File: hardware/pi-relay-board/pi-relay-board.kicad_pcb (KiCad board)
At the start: 2 copper layers, 101.9 x 59.1 mm, 41 parts, among them J1 Raspberry_Pi_2_3, J10 Conn_01x03_Socket, J11 Conn_01x03_Socket, J2 Conn_01x03_Socket, J3 Conn_01x03_Socket, J4 Conn_01x03_Socket, J5 Conn_01x03_Socket, J6 Conn_01x03_Socket, J7 Conn_01x03_Socket, J8 Conn_01x03_Socket, J9 Conn_01x03_Socket, K1 TIANBO-HJR-4102-L, K10 TIANBO-HJR-4102-L, K2 TIANBO-HJR-4102-L, K3 TIANBO-HJR-4102-L, K4 TIANBO-HJR-4102-L, K5 TIANBO-HJR-4102-L, K6 TIANBO-HJR-4102-L, K7 TIANBO-HJR-4102-L, K8 TIANBO-HJR-4102-L, K9 TIANBO-HJR-4102-L, Q11 BC847, Q12 BC847, Q13 BC847, Q14 BC847, Q15 BC847, Q16 BC847, Q17 BC847, Q18 BC847, Q19 BC847, Q20 BC847

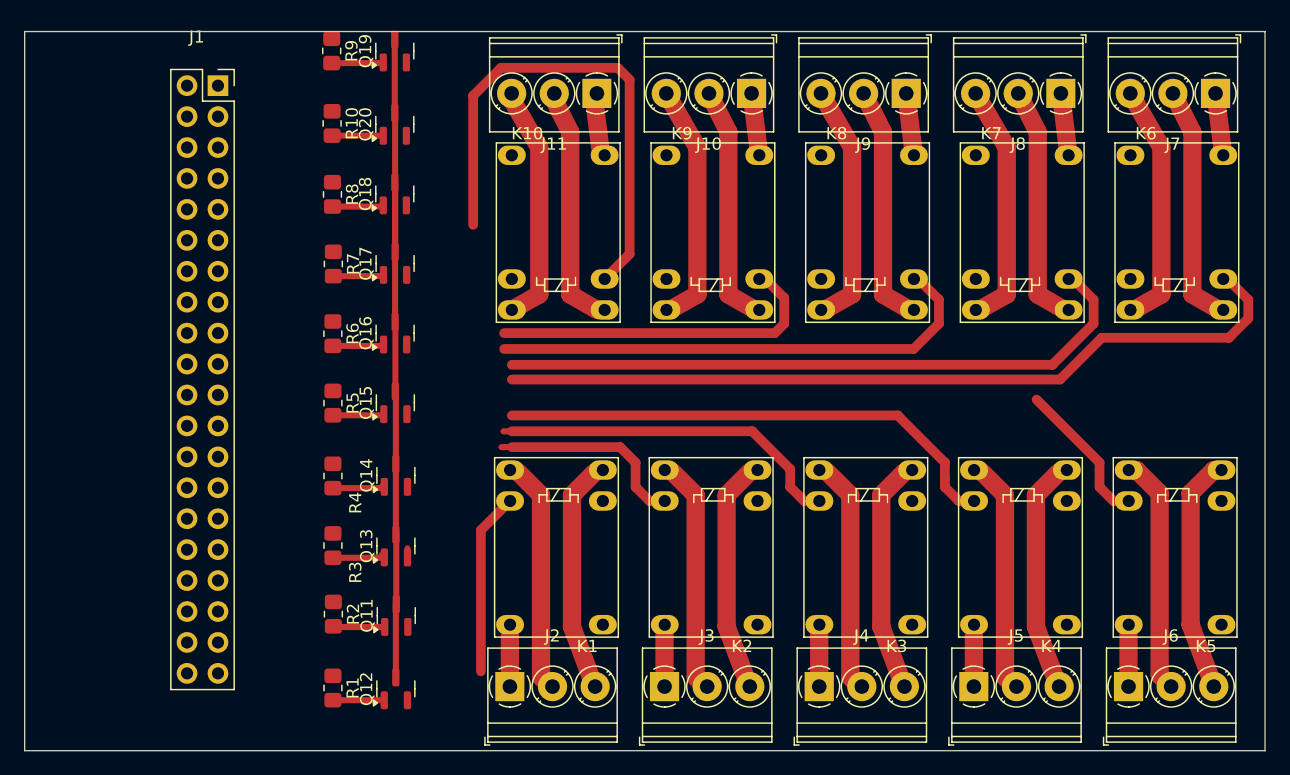
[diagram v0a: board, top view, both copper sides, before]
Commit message: hardware: change to tht
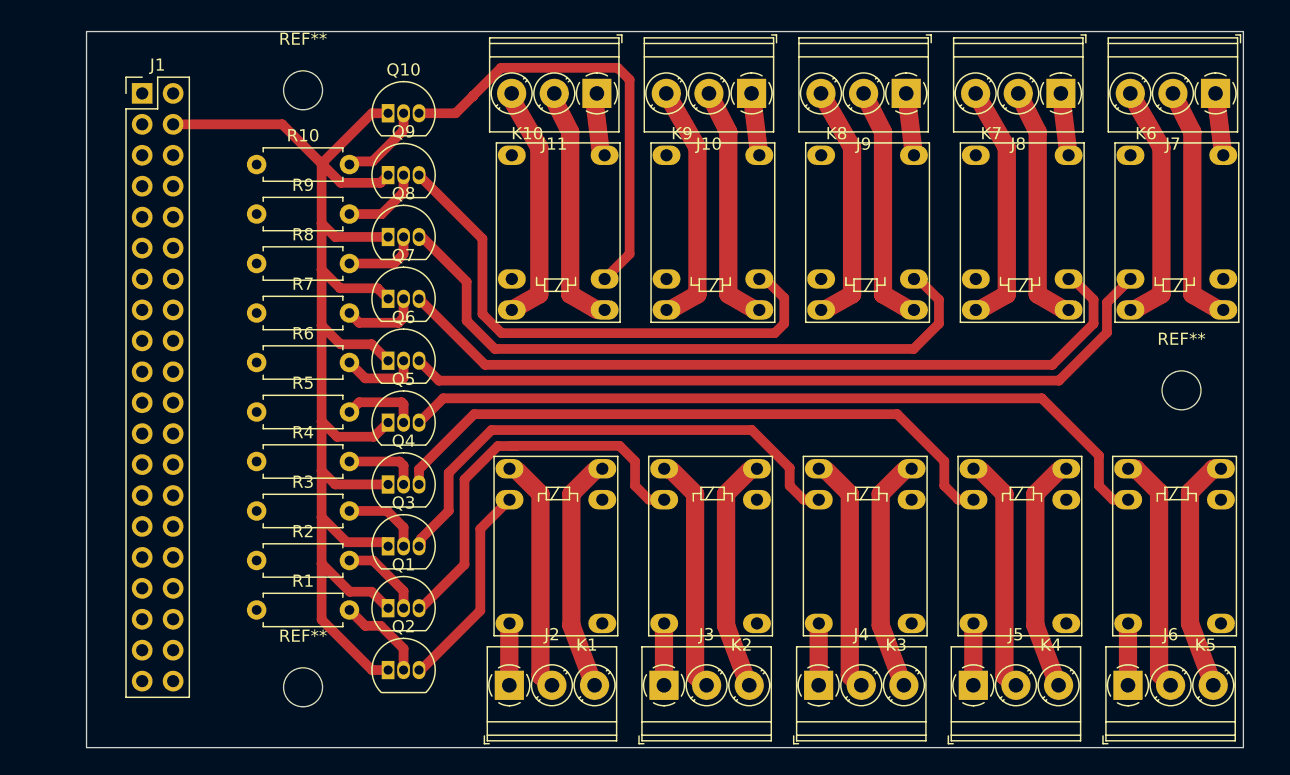
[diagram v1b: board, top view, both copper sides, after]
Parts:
- removed Q11, Q12, Q13, Q14, Q15, Q16, Q17, Q18, Q19, Q20: BC847, Package_TO_SOT_SMD:SOT-23
- added Q1: BC547, Package_TO_SOT_THT:TO-92_Inline, F.Cu at (173.4, 85.5)
- added Q10: BC547, Package_TO_SOT_THT:TO-92_Inline, F.Cu at (173.4, 44.8)
- added Q2: BC547, Package_TO_SOT_THT:TO-92_Inline, F.Cu at (173.4, 90.5)
- added Q3: BC547, Package_TO_SOT_THT:TO-92_Inline, F.Cu at (173.4, 80.4)
- added Q4: BC547, Package_TO_SOT_THT:TO-92_Inline, F.Cu at (173.4, 75.3)
- added Q5: BC547, Package_TO_SOT_THT:TO-92_Inline, F.Cu at (173.4, 70.2)
- added Q6: BC547, Package_TO_SOT_THT:TO-92_Inline, F.Cu at (173.4, 65.1)
- added Q7: BC547, Package_TO_SOT_THT:TO-92_Inline, F.Cu at (173.4, 60.0)
- added Q8: BC547, Package_TO_SOT_THT:TO-92_Inline, F.Cu at (173.4, 55.0)
- added Q9: BC547, Package_TO_SOT_THT:TO-92_Inline, F.Cu at (173.4, 49.9)
- added REF**: MountingHole_3.2mm_M3, MountingHole:MountingHole_3.2mm_M3, F.Cu at (166.4, 42.9)
- added REF**: MountingHole_3.2mm_M3, MountingHole:MountingHole_3.2mm_M3, F.Cu at (238.5, 67.6)
- added REF**: MountingHole_3.2mm_M3, MountingHole:MountingHole_3.2mm_M3, F.Cu at (166.4, 91.9)
- J1: footprint custom:Raspberry Connector -> Connector_PinHeader_2.54mm:PinHeader_2x20_P2.54mm_Vertical
- R1, R10, R2, R3, R4, R5, R6, R7, R8, R9: footprint Resistor_SMD:R_0805_2012Metric_Pad1.20x1.40mm_HandSolder -> Resistor_THT:R_Axial_DIN0207_L6.3mm_D2.5mm_P7.62mm_Horizontal
- moved J1 24.4 mm to (153.2, 43.2)
- moved R9 14.7 mm to (162.6, 53.1), turned to 0 degrees
- moved R1 8.96 mm to (162.6, 85.6), turned to 0 degrees
- moved R8 8.43 mm to (162.6, 57.1), turned to 0 degrees
- moved R2 7.69 mm to (162.6, 81.5), turned to 0 degrees
- moved R7 7.48 mm to (162.6, 61.2), turned to 0 degrees
- moved R10 7.05 mm to (162.6, 49.0), turned to 0 degrees
- moved R3 6.88 mm to (162.6, 77.5), turned to 0 degrees
- moved R6 6.69 mm to (162.6, 65.3), turned to 0 degrees
- moved R4 6.38 mm to (162.6, 73.4), turned to 0 degrees
- moved R5 6.31 mm to (162.6, 69.3), turned to 0 degrees
- moved J2 0.12 mm to (183.3, 91.8)
- moved J3 0.12 mm to (196.0, 91.8)
- moved J4 0.12 mm to (208.7, 91.8)
- moved J5 0.12 mm to (221.4, 91.8)
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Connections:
- J1 pad 11: /GPIO_1 -> /GPIO_5
- J1 pad 13: /GPIO_4 -> /GPIO_2
- J1 pad 15: /GPIO_3 -> /GPIO_6
- J1 pad 16: /GPIO_2 -> /GPIO
- J1 pad 18: /GPIO_7 -> /GPIO_8
- J1 pad 22: /GPIO_5 -> /GPIO_7
- J1 pad 29: /GPIO -> /GPIO_3
- J1 pad 31: /GPIO_8 -> /GPIO_4
- J1 pad 37: /GPIO_6 -> /GPIO_1
- K1 pad 5: unconnected-(K1-Pad5) -> Net-(Q2-E)
- K1 pad 8: Net-(Q12-E) -> Net-(Q2-E)
- K10 pad 5: unconnected-(K10-Pad5) -> Net-(Q10-E)
- K10 pad 8: Net-(Q20-E) -> Net-(Q10-E)
- K2 pad 5: unconnected-(K2-Pad5) -> Net-(Q1-E)
- K2 pad 8: Net-(Q11-E) -> Net-(Q1-E)
- K3 pad 5: unconnected-(K3-Pad5) -> Net-(Q3-E)
- K3 pad 8: Net-(Q13-E) -> Net-(Q3-E)
- K4 pad 5: unconnected-(K4-Pad5) -> Net-(Q4-E)
- K4 pad 8: Net-(Q14-E) -> Net-(Q4-E)
- K5 pad 5: unconnected-(K5-Pad5) -> Net-(Q5-E)
- K5 pad 8: Net-(Q15-E) -> Net-(Q5-E)
- K6 pad 5: unconnected-(K6-Pad5) -> Net-(Q6-E)
- K6 pad 8: Net-(Q16-E) -> Net-(Q6-E)
- K7 pad 5: unconnected-(K7-Pad5) -> Net-(Q7-E)
- K7 pad 8: Net-(Q17-E) -> Net-(Q7-E)
- K8 pad 5: unconnected-(K8-Pad5) -> Net-(Q8-E)
- K8 pad 8: Net-(Q18-E) -> Net-(Q8-E)
- K9 pad 5: unconnected-(K9-Pad5) -> Net-(Q9-E)
- K9 pad 8: Net-(Q19-E) -> Net-(Q9-E)
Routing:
- net Net-(Q16-E): track 66.8 -> 0.00 mm
- net Net-(Q6-E): track 0.00 -> 64.4 mm
- net Net-(Q5-E): track 0.00 -> 64.0 mm
- net Net-(Q7-E): track 0.00 -> 63.7 mm
- net +5V: track 58.2 -> 116.6 mm
- net Net-(Q17-E): track 53.9 -> 0.00 mm
- net Net-(Q8-E): track 0.00 -> 53.8 mm
- net Net-(Q4-E): track 0.00 -> 52.7 mm
- net Net-(Q9-E): track 0.00 -> 44.1 mm
- net Net-(Q20-E): track 42.7 -> 0.00 mm
- net Net-(Q3-E): track 0.00 -> 42.1 mm
- net Net-(Q14-E): track 42.0 -> 0.00 mm
- net Net-(Q18-E): track 41.3 -> 0.00 mm
- net Net-(Q10-E): track 0.00 -> 37.2 mm
- net Net-(Q1-E): track 0.00 -> 33.1 mm
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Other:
- board size 101.9 x 59.1 mm -> 95 x 58.8 mm

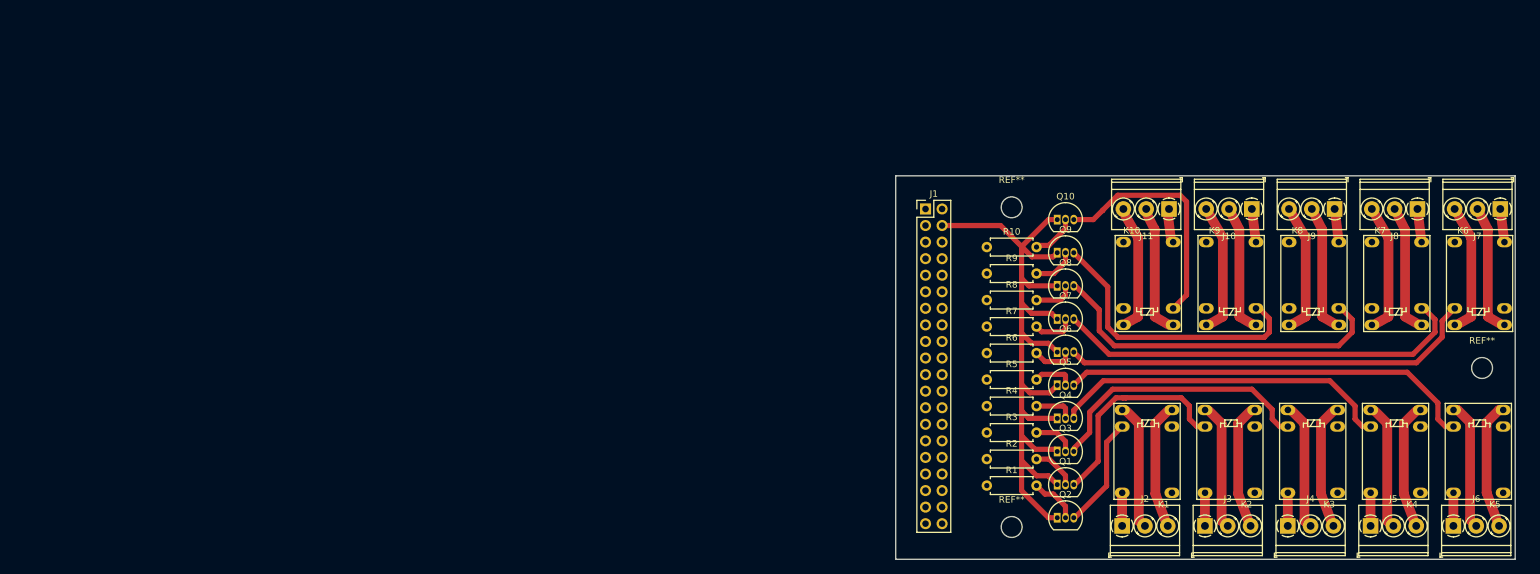
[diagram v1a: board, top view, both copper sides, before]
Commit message: feat: pcb bc547 footprint, laser image
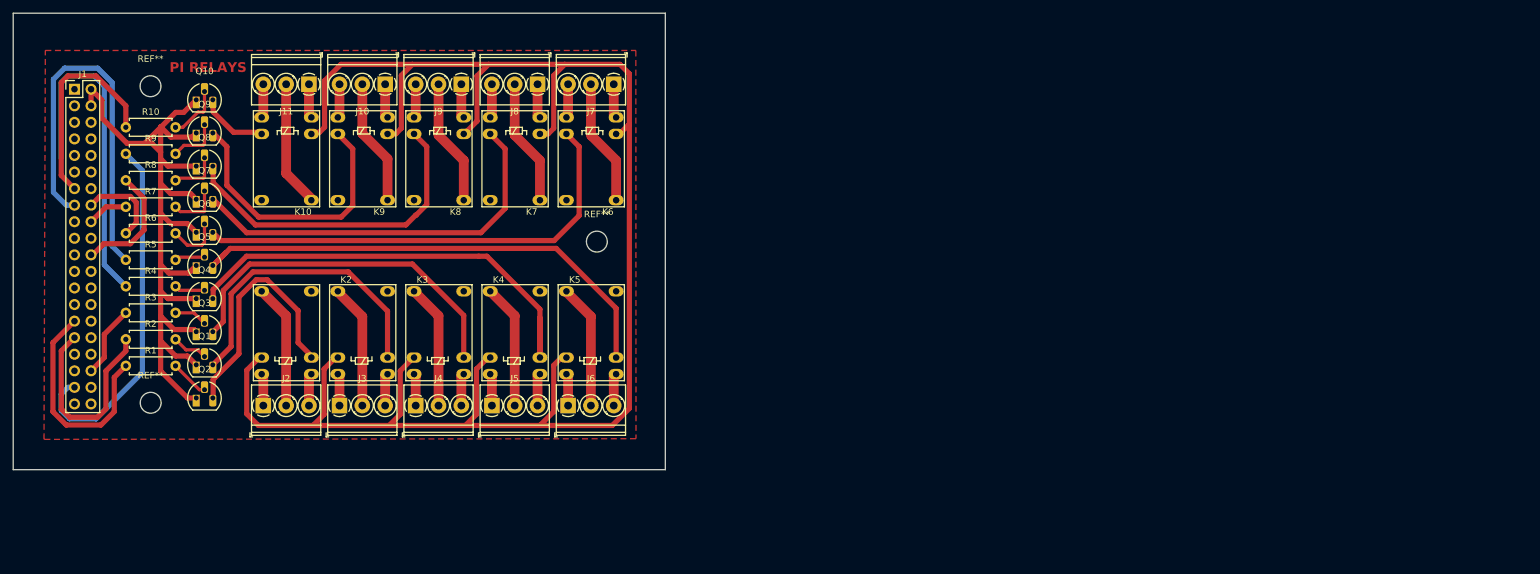
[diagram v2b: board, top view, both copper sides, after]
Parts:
- Q1, Q10, Q2, Q3, Q4, Q5, Q6, Q7, Q8, Q9: footprint Package_TO_SOT_THT:TO-92_Inline -> Package_TO_SOT_THT:TO-92_HandSolder
- moved K5 146.9 mm to (98.1, 55.8), turned to 0 degrees
- moved K4 145.9 mm to (86.4, 55.8), turned to 0 degrees
- moved K3 144.9 mm to (74.7, 55.8), turned to 0 degrees
- moved K2 144.0 mm to (63.0, 55.8), turned to 0 degrees
- moved K1 143.0 mm to (51.4, 55.8), turned to 0 degrees
- moved J7 137.3 mm to (105.3, 24.1)
- moved REF** 137.1 mm to (102.8, 48.2)
- moved J6 137.0 mm to (98.3, 73.3)
- moved J8 136.3 mm to (93.7, 24.1)
- moved J5 136.0 mm to (86.7, 73.3)
- moved J9 135.3 mm to (82.0, 24.1)
- moved J4 135.0 mm to (75.0, 73.3)
- moved J10 134.3 mm to (70.3, 24.1)
- moved J3 134.0 mm to (63.3, 73.3)
- moved REF** 133.4 mm to (34.3, 72.9)
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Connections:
- J1 pad 11: /GPIO_5 -> /Relay Pin 4/K
- J1 pad 13: /GPIO_2 -> /Relay Pin 10/K
- J1 pad 15: /GPIO_6 -> /Relay Pin 5/K
- J1 pad 16: /GPIO -> /Relay Pin 6/K
- J1 pad 18: /GPIO_8 -> /Relay Pin 7/K
- J1 pad 22: /GPIO_7 -> /Relay Pin 8/K
- J1 pad 29: /GPIO_3 -> /Relay Pin 1/K
- J1 pad 31: /GPIO_4 -> /Relay Pin 2/K
- J1 pad 37: /GPIO_1 -> /Relay Pin 9/K
- K1 pad 1: (no net) -> Net-(J2-Pin_2)
- K1 pad 12: Net-(J2-Pin_1) -> (no net)
- K1 pad 5: Net-(Q2-E) -> GND
- K1 pad 6: Net-(J2-Pin_3) -> Net-(J2-Pin_1)
- K1 pad 7: Net-(J2-Pin_2) -> Net-(J2-Pin_3)
- K10 pad 1: (no net) -> Net-(J11-Pin_2)
- K10 pad 12: Net-(J11-Pin_1) -> (no net)
- K10 pad 5: Net-(Q10-E) -> GND
- K10 pad 6: Net-(J11-Pin_3) -> Net-(J11-Pin_1)
- K10 pad 7: Net-(J11-Pin_2) -> Net-(J11-Pin_3)
- K2 pad 1: (no net) -> Net-(J3-Pin_2)
- K2 pad 12: Net-(J3-Pin_1) -> (no net)
- K2 pad 5: Net-(Q1-E) -> GND
- K2 pad 6: Net-(J3-Pin_3) -> Net-(J3-Pin_1)
- K2 pad 7: Net-(J3-Pin_2) -> Net-(J3-Pin_3)
- K3 pad 1: (no net) -> Net-(J4-Pin_2)
- K3 pad 12: Net-(J4-Pin_1) -> (no net)
- K3 pad 5: Net-(Q3-E) -> GND
- K3 pad 6: Net-(J4-Pin_3) -> Net-(J4-Pin_1)
- K3 pad 7: Net-(J4-Pin_2) -> Net-(J4-Pin_3)
- K4 pad 1: (no net) -> Net-(J5-Pin_2)
- K4 pad 12: Net-(J5-Pin_1) -> (no net)
- K4 pad 5: Net-(Q4-E) -> GND
- K4 pad 6: Net-(J5-Pin_3) -> Net-(J5-Pin_1)
- K4 pad 7: Net-(J5-Pin_2) -> Net-(J5-Pin_3)
- K5 pad 1: (no net) -> Net-(J6-Pin_2)
- K5 pad 12: Net-(J6-Pin_1) -> (no net)
- K5 pad 5: Net-(Q5-E) -> GND
- K5 pad 6: Net-(J6-Pin_3) -> Net-(J6-Pin_1)
- K5 pad 7: Net-(J6-Pin_2) -> Net-(J6-Pin_3)
- K6 pad 1: (no net) -> Net-(J7-Pin_2)
- K6 pad 12: Net-(J7-Pin_1) -> (no net)
- K6 pad 5: Net-(Q6-E) -> GND
- K6 pad 6: Net-(J7-Pin_3) -> Net-(J7-Pin_1)
- K6 pad 7: Net-(J7-Pin_2) -> Net-(J7-Pin_3)
- K7 pad 1: (no net) -> Net-(J8-Pin_2)
- K7 pad 12: Net-(J8-Pin_1) -> (no net)
- K7 pad 5: Net-(Q7-E) -> GND
- K7 pad 6: Net-(J8-Pin_3) -> Net-(J8-Pin_1)
- K7 pad 7: Net-(J8-Pin_2) -> Net-(J8-Pin_3)
- K8 pad 1: (no net) -> Net-(J9-Pin_2)
- K8 pad 12: Net-(J9-Pin_1) -> (no net)
- K8 pad 5: Net-(Q8-E) -> GND
- K8 pad 6: Net-(J9-Pin_3) -> Net-(J9-Pin_1)
- K8 pad 7: Net-(J9-Pin_2) -> Net-(J9-Pin_3)
- K9 pad 1: (no net) -> Net-(J10-Pin_2)
- K9 pad 12: Net-(J10-Pin_1) -> (no net)
- K9 pad 5: Net-(Q9-E) -> GND
- K9 pad 6: Net-(J10-Pin_3) -> Net-(J10-Pin_1)
- K9 pad 7: Net-(J10-Pin_2) -> Net-(J10-Pin_3)
- R1 pad 1: /Relay Pin 2/K1 -> /Relay Pin 1/K
- R10 pad 1: /Relay Pin 10/K1 -> /Relay Pin 10/K
- R2 pad 1: /Relay Pin 1/K1 -> /Relay Pin 2/K
- R3 pad 1: /Relay Pin 3/K1 -> /GPIO16
- R4 pad 1: /Relay Pin 4/K1 -> /Relay Pin 4/K
- R5 pad 1: /Relay Pin 5/K1 -> /Relay Pin 5/K
- R6 pad 1: /Relay Pin 6/K1 -> /Relay Pin 6/K
- R7 pad 1: /Relay Pin 7/K1 -> /Relay Pin 7/K
- R8 pad 1: /Relay Pin 8/K1 -> /Relay Pin 8/K
- R9 pad 1: /Relay Pin 9/K1 -> /Relay Pin 9/K
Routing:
- net GND: track 0.00 -> 269.3 mm
- net /Relay Pin 5/K: track 0.00 -> 60.1 mm
- net /Relay Pin 9/K: track 0.00 -> 55.5 mm
- net /Relay Pin 4/K: track 0.00 -> 51.4 mm
- net /Relay Pin 1/K: track 0.00 -> 34.1 mm
- net /Relay Pin 10/K: track 0.00 -> 32.6 mm
- net /Relay Pin 2/K: track 0.00 -> 31.6 mm
- net Net-(Q10-E): track 37.2 -> 10.6 mm
- net Net-(Q2-E): track 17.0 -> 37.2 mm
- net /Relay Pin 8/K: track 0.00 -> 18.5 mm
- net Net-(Q4-E): track 52.7 -> 70.5 mm
- net Net-(J7-Pin_3): track 20.1 -> 5.19 mm
- net Net-(J11-Pin_3): track 19.8 -> 5.19 mm
- net Net-(J9-Pin_3): track 19.8 -> 5.19 mm
- net Net-(J10-Pin_3): track 19.8 -> 5.19 mm
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- added copper zone on F.Cu, net GND
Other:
- board size 95 x 58.8 mm -> 100 x 70 mm
- board text added: "PI RELAYS"

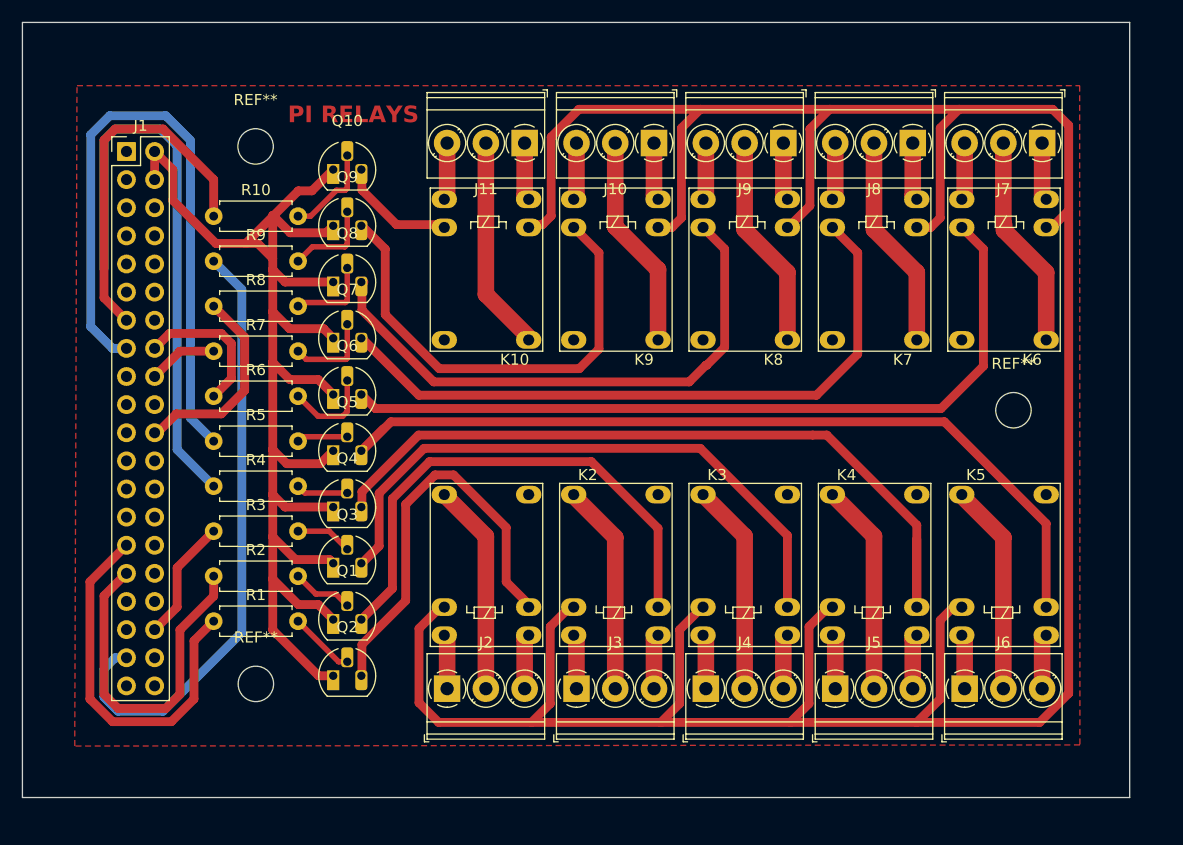
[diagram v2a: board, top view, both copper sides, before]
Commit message: fix: laser image scaling
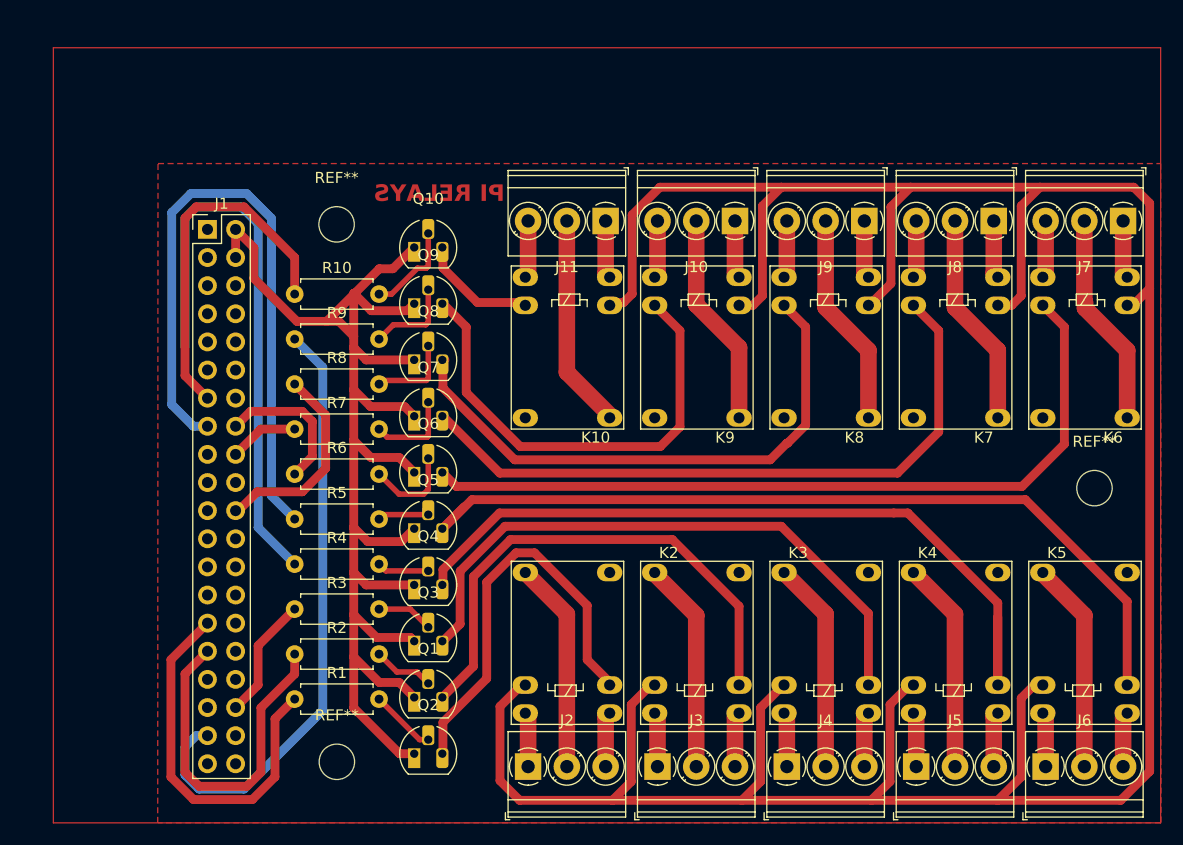
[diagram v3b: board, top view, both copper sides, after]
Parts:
- moved J7 10.1 mm to (112.7, 31.1)
- moved J8 10.1 mm to (101.0, 31.1)
- moved J9 10.1 mm to (89.3, 31.1)
- moved K6 10.1 mm to (113.0, 48.9)
- moved K7 10.1 mm to (101.3, 48.9)
- moved K8 10.1 mm to (89.7, 48.9)
- moved REF** 10.1 mm to (41.6, 31.4)
- moved REF** 10.1 mm to (41.7, 79.9)
- moved J1 10.1 mm to (30.0, 31.9)
- moved J11 10.1 mm to (65.9, 31.1)
- moved K10 10.1 mm to (66.3, 48.9)
- moved Q10 10.1 mm to (48.6, 33.5)
- moved Q3 10.1 mm to (48.6, 69.0)
- moved Q5 10.1 mm to (48.6, 58.9)
- moved Q6 10.1 mm to (48.6, 53.8)
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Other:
- board outline removed
